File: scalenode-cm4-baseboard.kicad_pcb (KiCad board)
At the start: 4 copper layers, 128.5 x 40 mm, 147 parts, among them IC1 TPS2378DDA, J1 B2B-XH-A_LF__SN_, J10 LSHM-130-01-L-RH-A-S-K-TR, J3 1-2199230-6, J4 1140084168, J5 0473460001, J6 SS-74800-144, J7 DF40HC(3.0)-100DS-0.4v, J8 DF40HC(3.0)-100DS-0.4v, Q6 BSS138-7-F, U1 TS3USB30EDGSR, U2 AP62301WU-7, U3 TPS2373-3RGW, U4 URB4805YMD-30WR3, U5 TS3USB30EDGSR, U6 FT234XD-R

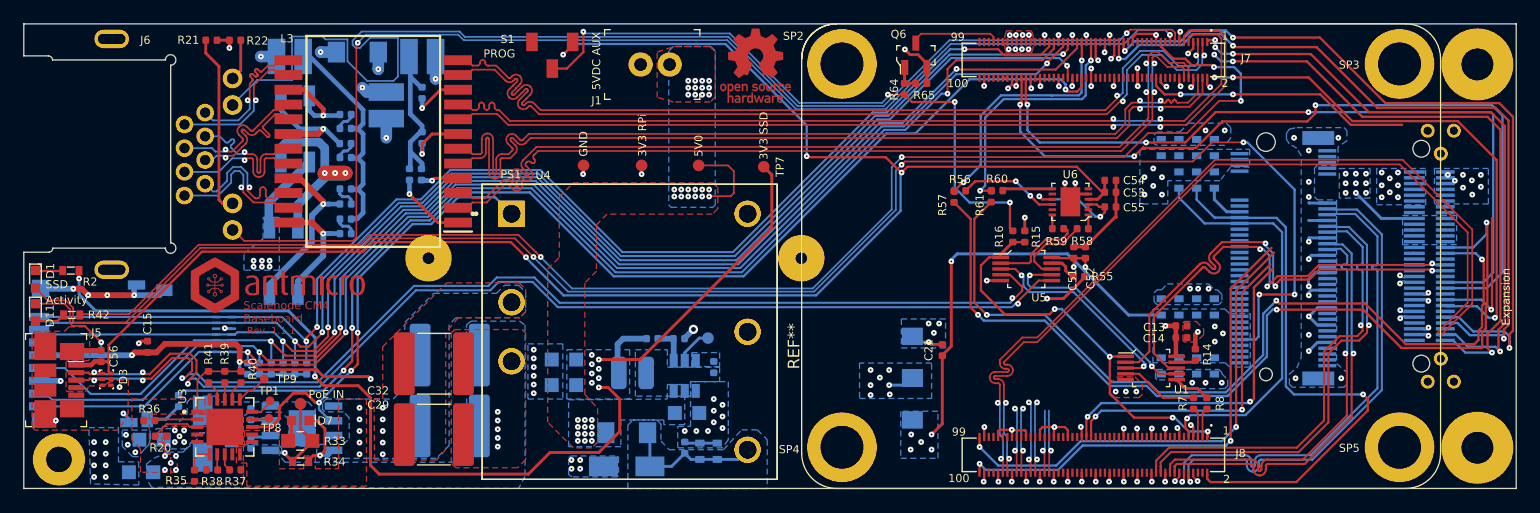
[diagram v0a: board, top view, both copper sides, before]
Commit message: Reroute high speed signals and GPIO signals
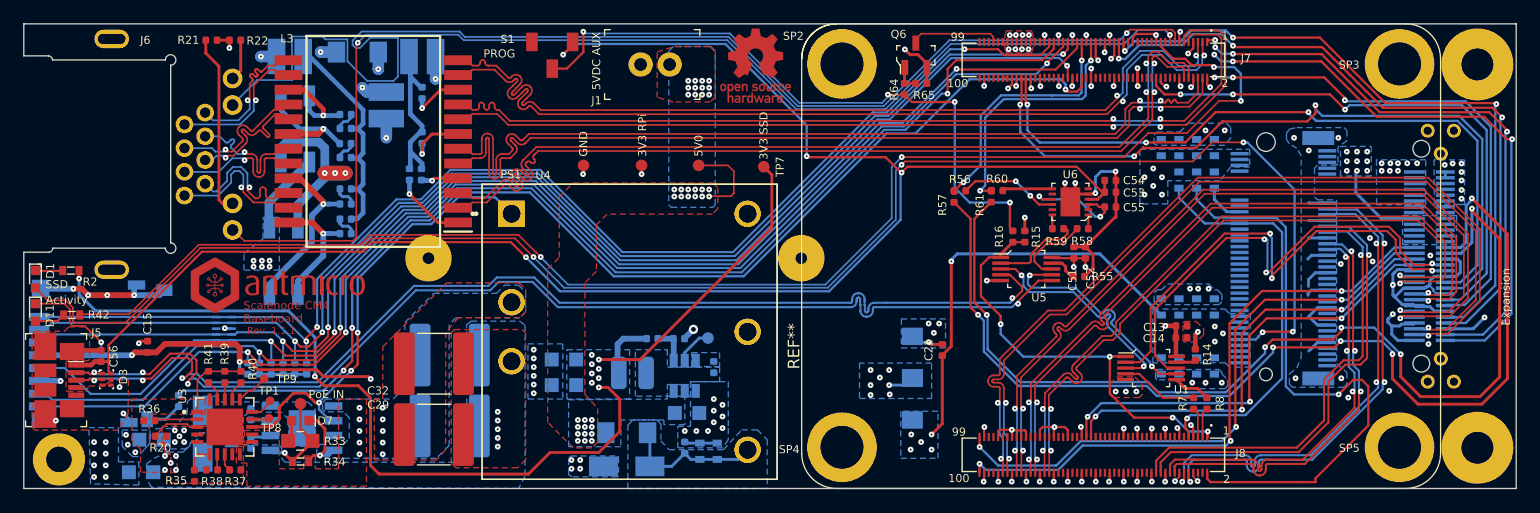
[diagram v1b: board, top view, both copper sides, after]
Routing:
- net HDMI0_D0_N: track 7.88 -> 70.9 mm
- net HDMI0_D0_P: track 7.04 -> 68.4 mm
- net HDMI0_D1_N: track 7.57 -> 62.1 mm
- net HDMI0_D1_P: track 7.57 -> 60.3 mm
- net HDMI0_D2_N: track 6.82 -> 59.3 mm, vias 2 -> 3
- net HDMI0_D2_P: track 6.82 -> 57.6 mm, vias 2 -> 3
- net GND: track 123.2 -> 159.8 mm, vias 123 -> 125
- net Adapter_TXD: track 73.4 -> 87.5 mm, vias 3 -> 5
- net GPIO26: track 35.5 -> 47.9 mm
- net HDMI0_SCL: track 41.8 -> 52.5 mm, vias 2 -> 3
- net Adapter_RXD: track 79.4 -> 90.0 mm, vias 3 -> 5
- net HDMI0_CEC: track 28.3 -> 38.9 mm, vias 2 -> 3
- net HDMI0_SDA: track 41.4 -> 51.6 mm, vias 2 -> 3
- net HDMI0_HOTPLUG: track 28.6 -> 38.7 mm, vias 2 -> 3
- net GPIO7: track 65.3 -> 57.3 mm
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- added copper zone on In2.Cu, net GND

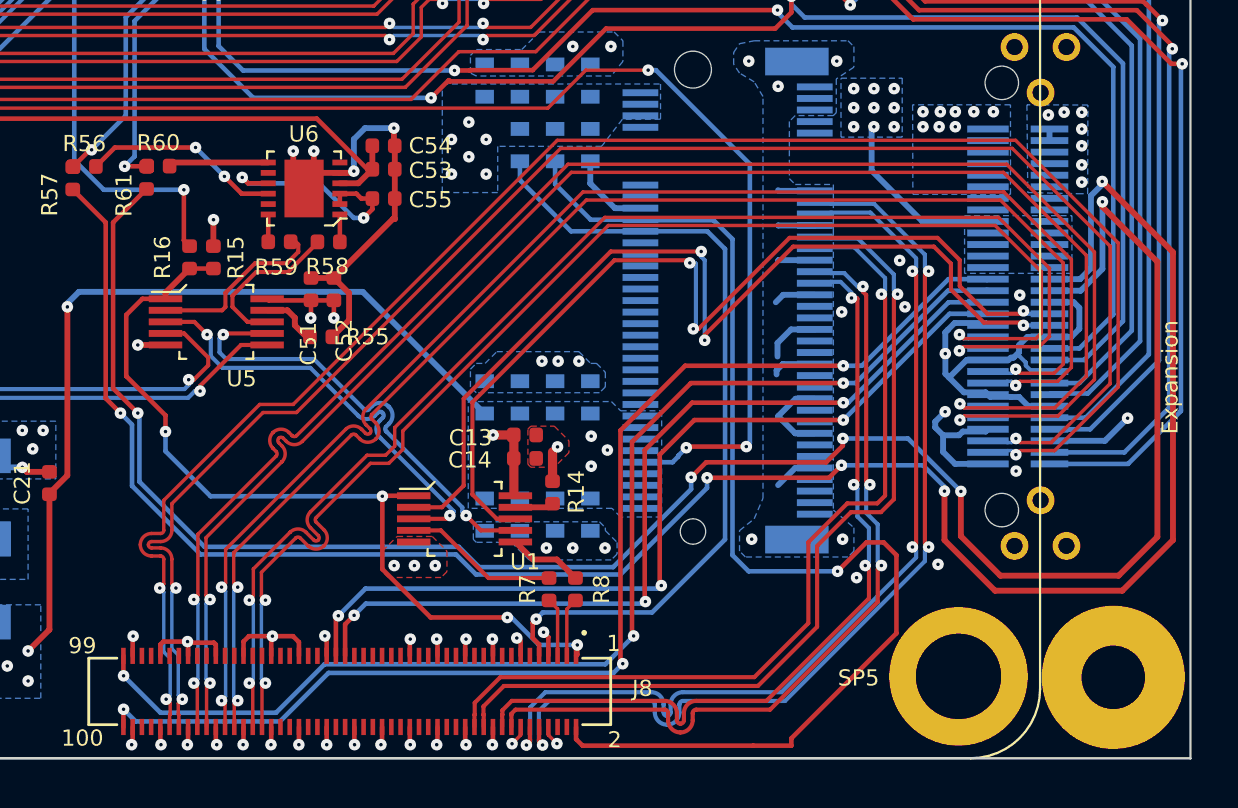
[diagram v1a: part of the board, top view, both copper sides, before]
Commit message: Tune high speed signals
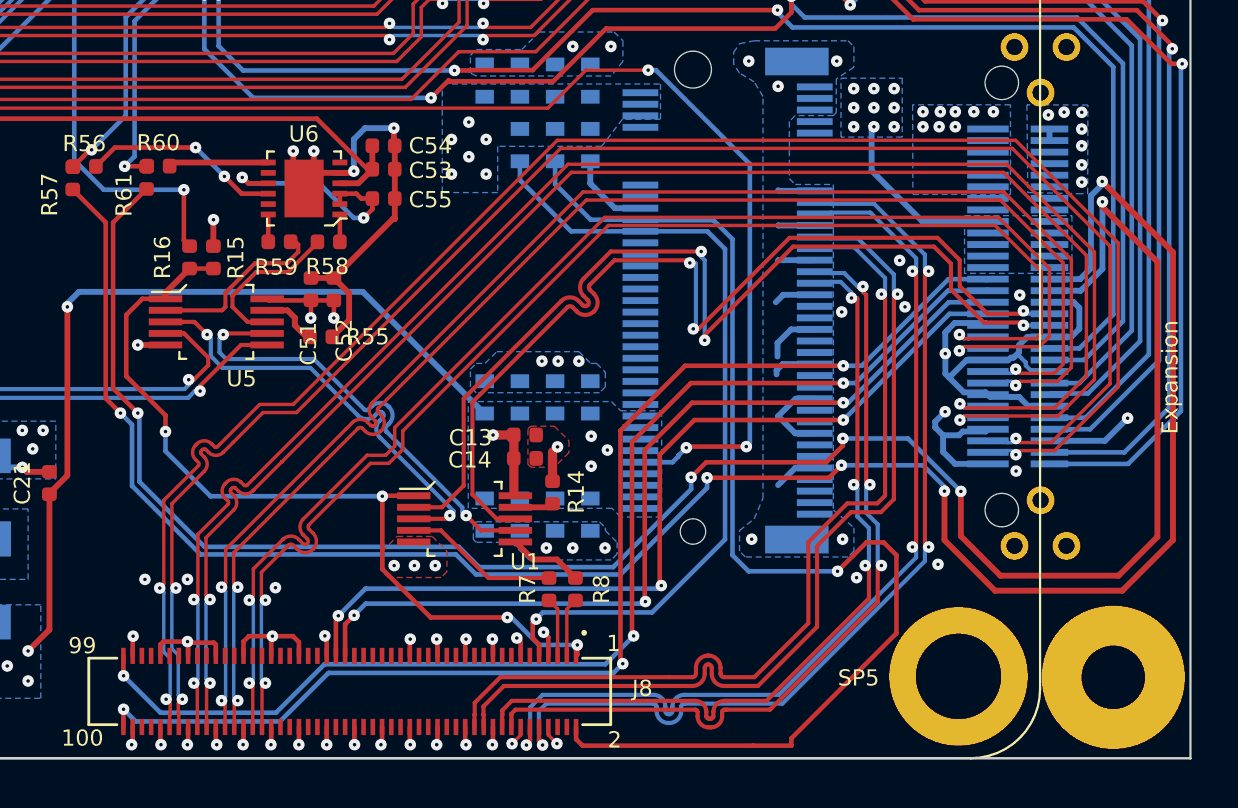
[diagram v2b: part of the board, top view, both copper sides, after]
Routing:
- net Adapter_USB_N: track 40.6 -> 41.9 mm
- net Adapter_USB_P: track 42.1 -> 43.4 mm
- net PCIE_TX_N: track 37.1 -> 38.3 mm
- net PCIE_TX_P: track 37.7 -> 38.9 mm
- net HDMI0_CK_N: track 74.5 -> 74.0 mm
- net HDMI0_CK_P: track 72.8 -> 72.2 mm
- net GND: vias 125 -> 128

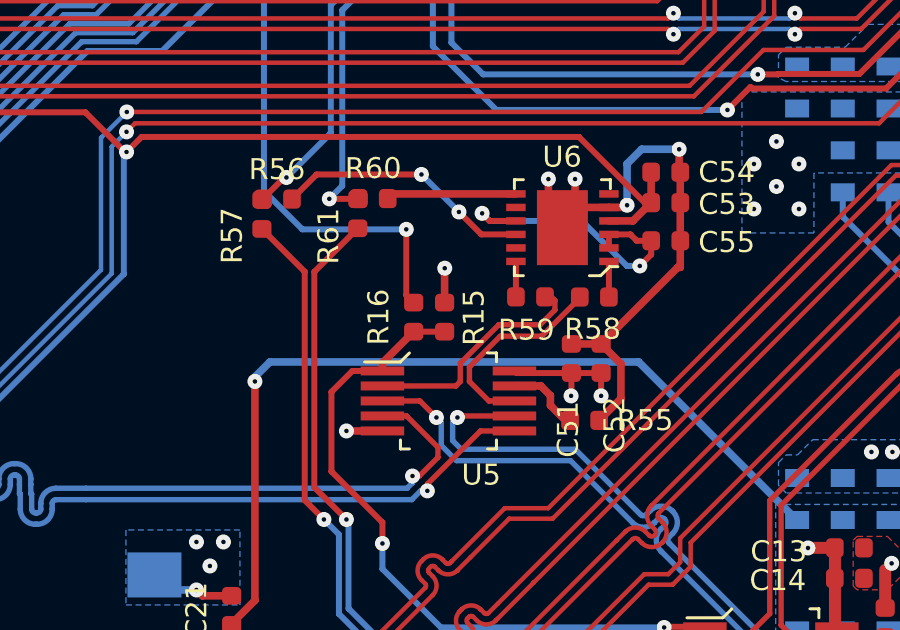
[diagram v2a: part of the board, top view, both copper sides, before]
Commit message: Tune ftdi_usb signal
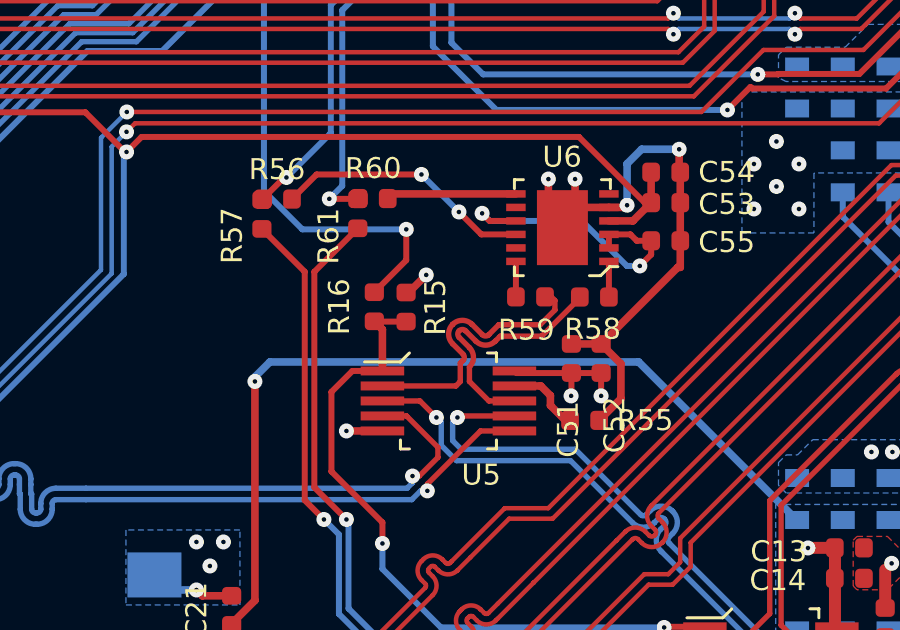
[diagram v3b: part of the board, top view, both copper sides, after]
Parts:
- moved R16 1.36 mm to (158.9, 74.7)
- moved R15 1.33 mm to (160.0, 74.7)
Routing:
- net /Interfaces/FTDI_USB_P: track 7.86 -> 9.47 mm
- net /Interfaces/FTDI_USB_N: track 6.92 -> 8.54 mm

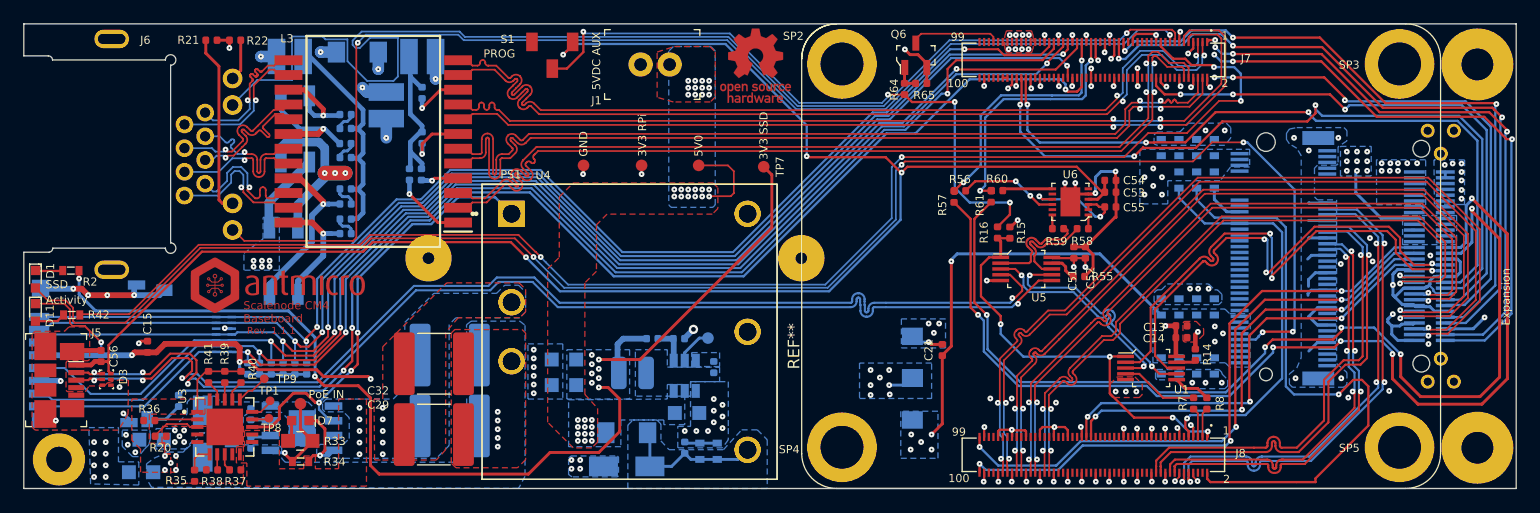
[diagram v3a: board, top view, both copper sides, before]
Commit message: Add gnd plane next to PCIe vias
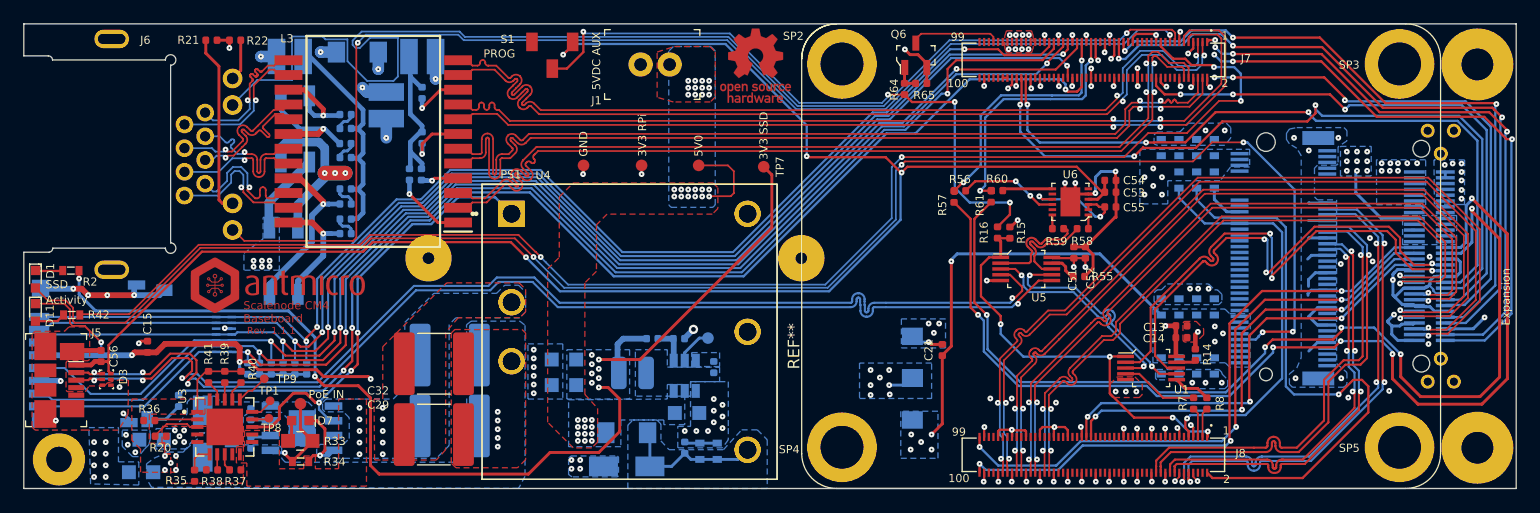
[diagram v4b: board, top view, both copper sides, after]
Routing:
- net PCIE_CLK_nREQ: track 51.6 -> 50.1 mm
- net SD_DAT1: track 112.2 -> 112.7 mm
